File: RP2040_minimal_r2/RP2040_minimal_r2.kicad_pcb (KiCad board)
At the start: 2 copper layers, 52 x 51 mm, 34 parts, among them J1 USB_B_Micro, J2 Conn_01x02, J3 Conn_02x18_Odd_Even, J4 Conn_02x18_Odd_Even, U1 NCP1117-3.3_SOT223, U2 W25Q128JVS, U3 RP2040, Y1 ABM8-272-T3

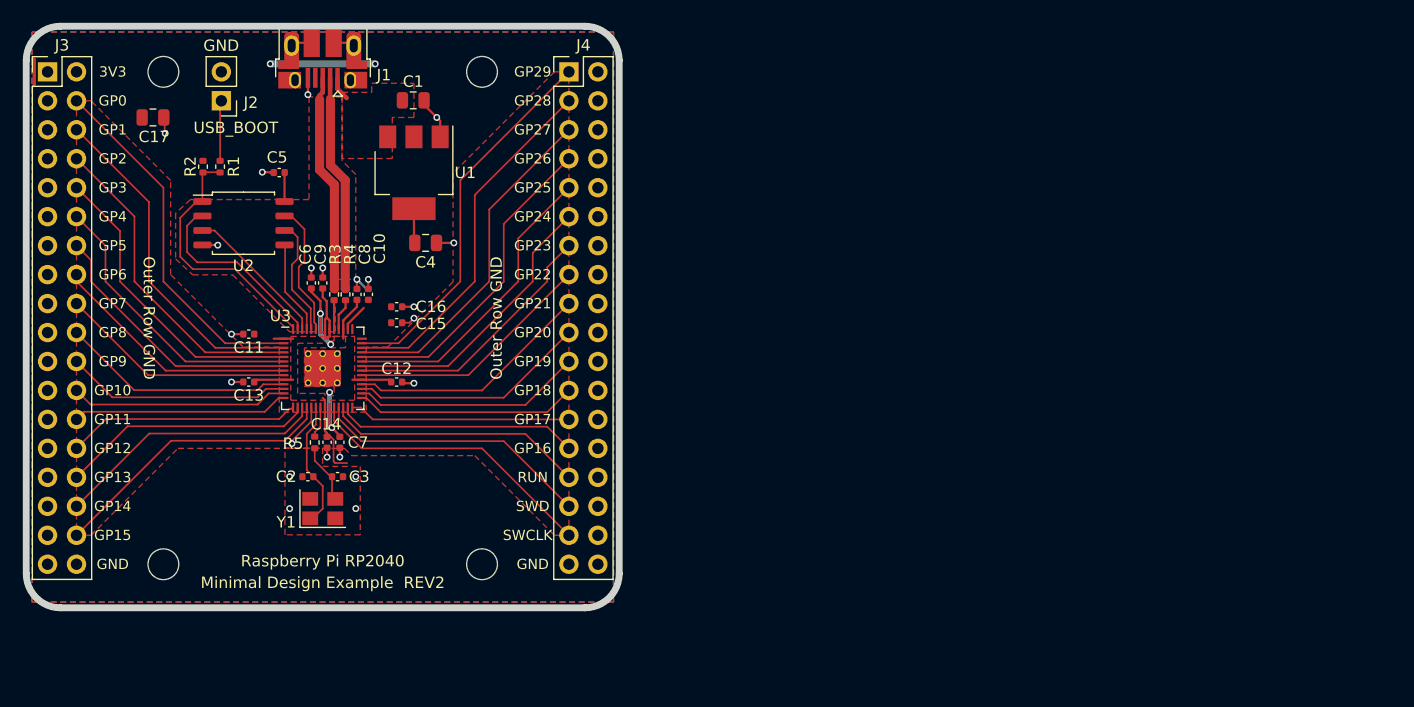
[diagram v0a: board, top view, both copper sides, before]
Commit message: Reshape board to 46x34mm to match the footprint of the old breadboard. Replace some components (voltage regulator, flash memory chip, crystal) with ones that are cheaper and/or smaller Add BOOT/RESET buttons Add SMD piezo speaker add 3 SPI connectors (JST-GH 1.25mm pitch 6 pin). Lots of routing etc.
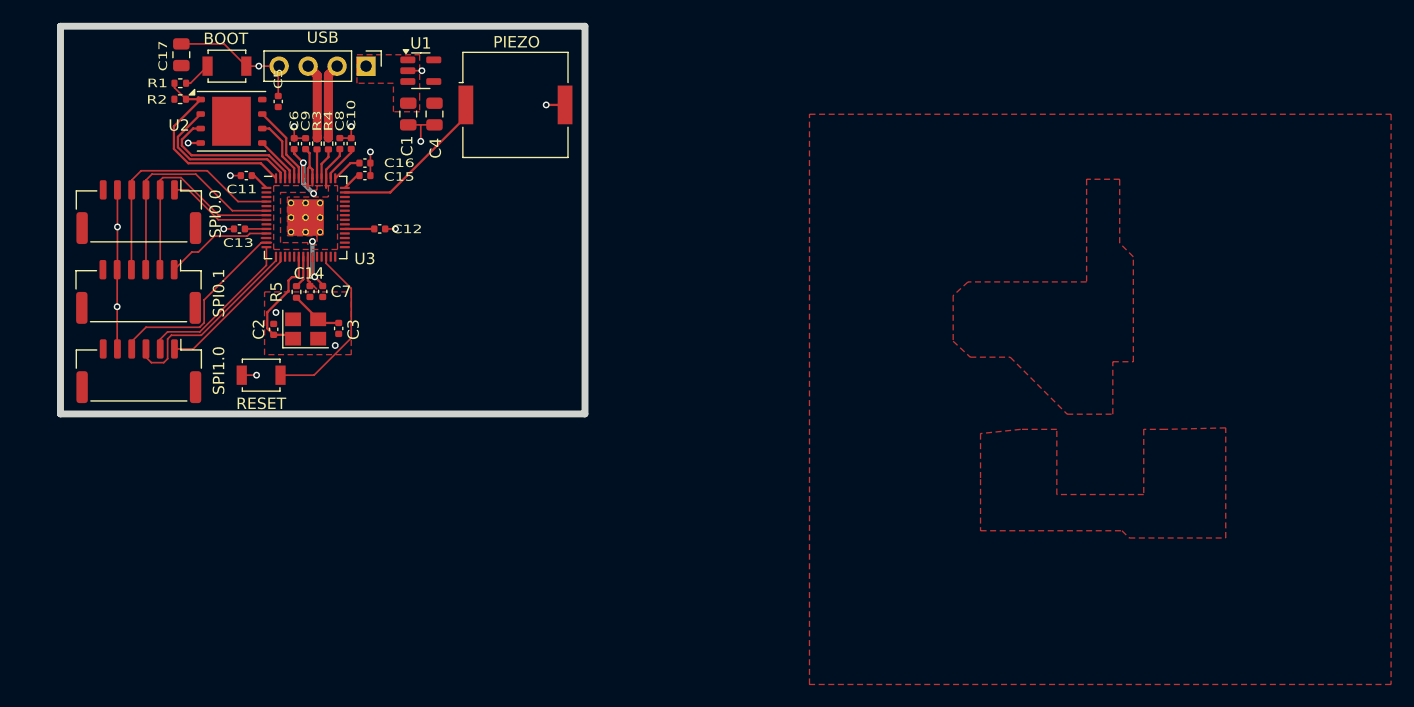
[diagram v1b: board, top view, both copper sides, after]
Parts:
- removed H1, H2, H3, H4: MountingHole, MountingHole:MountingHole_2.7mm_M2.5
- removed J4: Conn_02x18_Odd_Even, Connector_PinHeader_2.54mm:PinHeader_2x18_P2.54mm_Vertical
- added J5: USB, Connector_PinHeader_2.54mm:PinHeader_1x04_P2.54mm_Vertical, F.Cu at (103.8, 73.5)
- added LS1: PIEZO, Buzzer_Beeper:Buzzer_Murata_PKMCS0909E, F.Cu at (116.9, 76.9)
- added SW1: BOOT, Button_Switch_SMD:SW_SPST_B3U-1000P, F.Cu at (91.6, 73.5)
- added SW2: RESET, Button_Switch_SMD:SW_SPST_B3U-1000P, F.Cu at (94.6, 100.6)
- J1: value USB_B_Micro -> SPI0.0; footprint RP2040_minimal:USB_Micro-B_Amphenol_10103594-0001LF_Horizontal_modified -> Connector_JST:JST_GH_BM06B-GHS-TBT_1x06-1MP_P1.25mm_Vertical
- J2: value Conn_01x02 -> SPI0.1; footprint Connector_PinHeader_2.54mm:PinHeader_1x02_P2.54mm_Vertical -> Connector_JST:JST_GH_BM06B-GHS-TBT_1x06-1MP_P1.25mm_Vertical
- J3: value Conn_02x18_Odd_Even -> SPI1.0; footprint Connector_PinHeader_2.54mm:PinHeader_2x18_P2.54mm_Vertical -> Connector_JST:JST_GH_BM06B-GHS-TBT_1x06-1MP_P1.25mm_Vertical
- U1: value NCP1117-3.3_SOT223 -> AP2112K-3.3TRG1; footprint Package_TO_SOT_SMD:SOT-223-3_TabPin2 -> Package_TO_SOT_SMD:SOT-23-5
- U2: footprint Package_SO:SOIC-8_5.23x5.23mm_P1.27mm -> Package_SON:WSON-8-1EP_6x5mm_P1.27mm_EP3.4x4.3mm
- Y1: value ABM8-272-T3 -> X322512MSB4SI
- moved J3 27.4 mm to (83.9, 100.2), turned to 180 degrees
- moved J1 21.8 mm to (83.9, 86.3)
- moved J2 18.3 mm to (83.8, 93.3)
- moved Y1 15.8 mm to (98.5, 96.5)
- moved C11 13.9 mm to (93.3, 83.1)
- moved C12 13.5 mm to (105.0, 87.8)
- moved C13 13.4 mm to (92.7, 87.8)
- moved C10 13.3 mm to (102.5, 80.3)
- moved C14 13.3 mm to (98.9, 93.3)
- moved C7 13.3 mm to (100.0, 93.3)
- moved C8 13.3 mm to (101.5, 80.3)
- moved R3 13.3 mm to (99.5, 80.3)
- moved R4 13.3 mm to (100.5, 80.3)
- moved U3 13.3 mm to (98.5, 86.8)
- moved R5 13.3 mm to (97.7, 93.3)
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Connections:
- J1 pad 1: VBUS -> NCS0.0
- J1 pad 2: /USB_D- -> MOSI
- J1 pad 3: /USB_D+ -> MISO
- J1 pad 4: unconnected-(J1-ID-Pad4) -> SCLK
- J1 pad 6: GND -> +3V3
- J2 pad 1: /~{USB_BOOT} -> NCS0.1
- J2 pad 2: GND -> MOSI
- J3 pad 1: GND -> NCS1.0
- J3 pad 2: +3V3 -> MOSI1
- J3 pad 3: GND -> MISO1
- J3 pad 4: /GPIO0 -> SCLK1
- J3 pad 6: /GPIO1 -> +3V3
- R1 pad 2: /~{USB_BOOT} -> Net-(R1-Pad2)
- U1 pad 1: GND -> VBUS
- U1 pad 2: +3V3 -> GND
- U3 pad 11: /GPIO8 -> NCS0.1
- U3 pad 12: /GPIO9 -> unconnected-(U3-GPIO9-Pad12)
- U3 pad 13: /GPIO10 -> SCLK1
- U3 pad 14: /GPIO11 -> MOSI1
- U3 pad 15: /GPIO12 -> MISO1
- U3 pad 16: /GPIO13 -> NCS1.0
- U3 pad 17: /GPIO14 -> unconnected-(U3-GPIO14-Pad17)
- U3 pad 18: /GPIO15 -> unconnected-(U3-GPIO15-Pad18)
- U3 pad 2: /GPIO0 -> unconnected-(U3-GPIO0-Pad2)
- U3 pad 27: /GPIO16 -> unconnected-(U3-GPIO16-Pad27)
- U3 pad 28: /GPIO17 -> unconnected-(U3-GPIO17-Pad28)
- U3 pad 29: /GPIO18 -> unconnected-(U3-GPIO18-Pad29)
- U3 pad 3: /GPIO1 -> unconnected-(U3-GPIO1-Pad3)
- U3 pad 30: /GPIO19 -> unconnected-(U3-GPIO19-Pad30)
- U3 pad 31: /GPIO20 -> unconnected-(U3-GPIO20-Pad31)
- U3 pad 32: /GPIO21 -> unconnected-(U3-GPIO21-Pad32)
- U3 pad 34: /GPIO22 -> unconnected-(U3-GPIO22-Pad34)
- U3 pad 35: /GPIO23 -> unconnected-(U3-GPIO23-Pad35)
- U3 pad 36: /GPIO24 -> unconnected-(U3-GPIO24-Pad36)
- U3 pad 37: /GPIO25 -> unconnected-(U3-GPIO25-Pad37)
- U3 pad 38: /GPIO26_ADC0 -> unconnected-(U3-GPIO26_ADC0-Pad38)
- U3 pad 39: /GPIO27_ADC1 -> unconnected-(U3-GPIO27_ADC1-Pad39)
- U3 pad 4: /GPIO2 -> SCLK
- U3 pad 40: /GPIO28_ADC2 -> unconnected-(U3-GPIO28_ADC2-Pad40)
- U3 pad 41: /GPIO29_ADC3 -> /PIEZO
- U3 pad 5: /GPIO3 -> unconnected-(U3-GPIO3-Pad5)
- U3 pad 6: /GPIO4 -> MISO
- U3 pad 7: /GPIO5 -> MOSI
- U3 pad 8: /GPIO6 -> NCS0.0
- U3 pad 9: /GPIO7 -> unconnected-(U3-GPIO7-Pad9)
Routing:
- net /GPIO29_ADC3: track 33.2 -> 0.00 mm
- net /GPIO0: track 31.8 -> 0.00 mm
- net /GPIO28_ADC2: track 31.6 -> 0.00 mm
- net /GPIO1: track 30.2 -> 0.00 mm
- net /GPIO27_ADC1: track 29.9 -> 0.00 mm
- net /GPIO2: track 28.5 -> 0.00 mm
- net /GPIO26_ADC0: track 28.3 -> 0.00 mm
- net /GPIO3: track 26.9 -> 0.00 mm
- net /GPIO25: track 26.7 -> 0.00 mm
- net /SWCLK: track 25.9 -> 0.00 mm
- net /GPIO15: track 25.4 -> 0.00 mm
- net /GPIO4: track 25.3 -> 0.00 mm
- net /GPIO24: track 25.0 -> 0.00 mm
- net /SWD: track 24.3 -> 0.00 mm
- net /GPIO14: track 23.8 -> 0.00 mm
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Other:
- board size 52 x 51 mm -> 46 x 34 mm
- board text removed: "3V3"
- board text removed: "GND"
- board text removed: "GP0"
- board text removed: "GP1"
- board text removed: "GP10"
- board text removed: "GP11"
- board text removed: "GP12"
- board text removed: "GP13"
- board text removed: "GP14"
- board text removed: "GP15"
- board text removed: "GP16"
- board text removed: "GP17"
- board text removed: "GP18"
- board text removed: "GP19"
- board text removed: "GP2"
- board text removed: "GP20"
- board text removed: "GP21"
- board text removed: "GP22"
- board text removed: "GP23"
- board text removed: "GP24"
- board text removed: "GP25"
- board text removed: "GP26"
- board text removed: "GP27"
- board text removed: "GP28"
- board text removed: "GP29"
- board text removed: "GP3"
- board text removed: "GP4"
- board text removed: "GP5"
- board text removed: "GP6"
- board text removed: "GP7"
- board text removed: "GP8"
- board text removed: "GP9"
- board text removed: "Minimal Design Example REV2"
- board text removed: "Outer Row GND"
- board text removed: "RUN"
- board text removed: "Raspberry Pi RP2040"
- board text removed: "SWCLK"
- board text removed: "SWD"
- board text removed: "USB_BOOT"

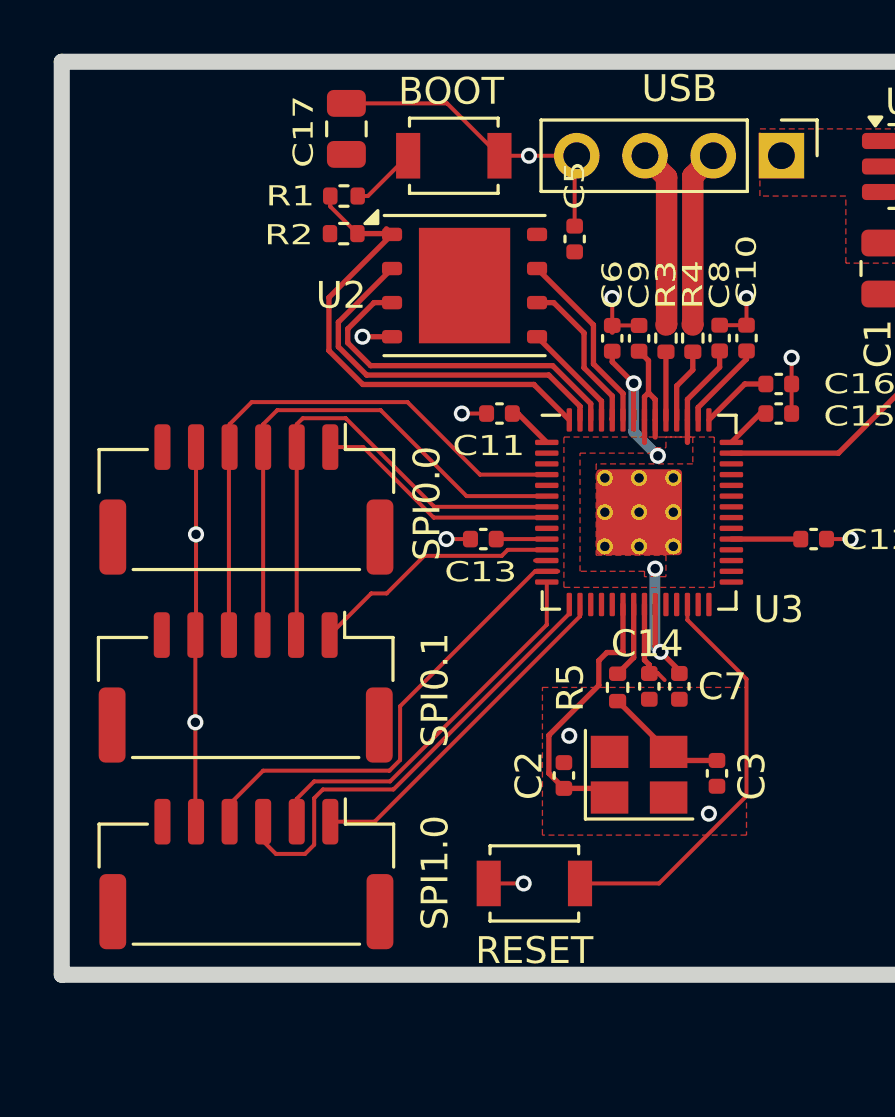
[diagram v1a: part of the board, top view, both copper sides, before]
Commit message: Change connectors to JST-SH 1.0mm Additional routing tweaks.
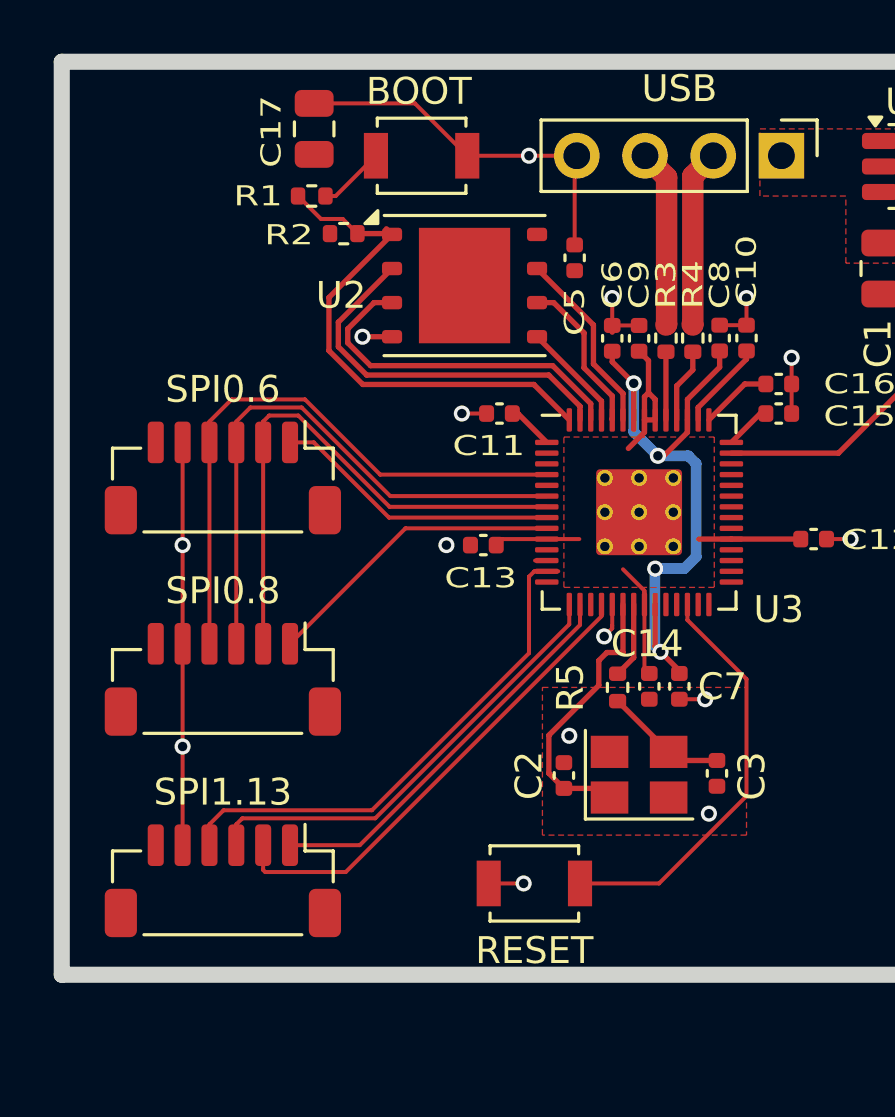
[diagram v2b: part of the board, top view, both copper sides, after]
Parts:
- J1: value SPI0.0 -> SPI0.6; footprint Connector_JST:JST_GH_BM06B-GHS-TBT_1x06-1MP_P1.25mm_Vertical -> Connector_JST:JST_SH_BM06B-SRSS-TB_1x06-1MP_P1.00mm_Vertical
- J2: value SPI0.1 -> SPI0.8; footprint Connector_JST:JST_GH_BM06B-GHS-TBT_1x06-1MP_P1.25mm_Vertical -> Connector_JST:JST_SH_BM06B-SRSS-TB_1x06-1MP_P1.00mm_Vertical
- J3: value SPI1.0 -> SPI1.13; footprint Connector_JST:JST_GH_BM06B-GHS-TBT_1x06-1MP_P1.25mm_Vertical -> Connector_JST:JST_SH_BM06B-SRSS-TB_1x06-1MP_P1.00mm_Vertical
- moved R1 1.20 mm to (86.3, 75.0)
- moved C17 1.20 mm to (86.4, 72.5)
- moved SW1 1.20 mm to (90.4, 73.5)
- moved J1 1.19 mm to (83.0, 85.5)
- moved J3 0.91 mm to (83.0, 100.5)
- moved J2 0.90 mm to (83.0, 93.0)
- moved C5 0.70 mm to (96.1, 77.3)
- moved C13 0.22 mm to (92.7, 88.0)
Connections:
- net NCS0.0 renamed NCS06
- net NCS1.0 renamed NCS13
- J2 pad 1: NCS0.1 -> NCS07
- U3 pad 11: NCS0.1 -> unconnected-(U3-GPIO8-Pad11)
- U3 pad 14: MOSI1 -> unconnected-(U3-GPIO11-Pad14)
- U3 pad 18: unconnected-(U3-GPIO15-Pad18) -> MOSI1
- U3 pad 9: unconnected-(U3-GPIO7-Pad9) -> NCS07
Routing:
- net NCS07: track 0.00 -> 11.3 mm
- net NCS0.1: track 9.40 -> 0.00 mm
- net +1V1: track 16.0 -> 23.8 mm
- net GND: track 44.5 -> 48.7 mm, vias 16 -> 18
- net MOSI1: track 14.4 -> 17.9 mm
- net +3V3: track 23.0 -> 26.3 mm
- net NCS13: track 12.9 -> 15.0 mm
- net SCLK1: track 17.7 -> 19.3 mm
- net MOSI: track 18.7 -> 20.3 mm
- net NCS06: track 9.15 -> 10.7 mm
- net MISO: track 20.0 -> 21.4 mm
- net SCLK: track 21.2 -> 22.3 mm
- net /QSPI_SS: track 19.0 -> 19.9 mm
- net MISO1: track 16.7 -> 17.3 mm
- removed copper zone on F.Cu, net +1V1

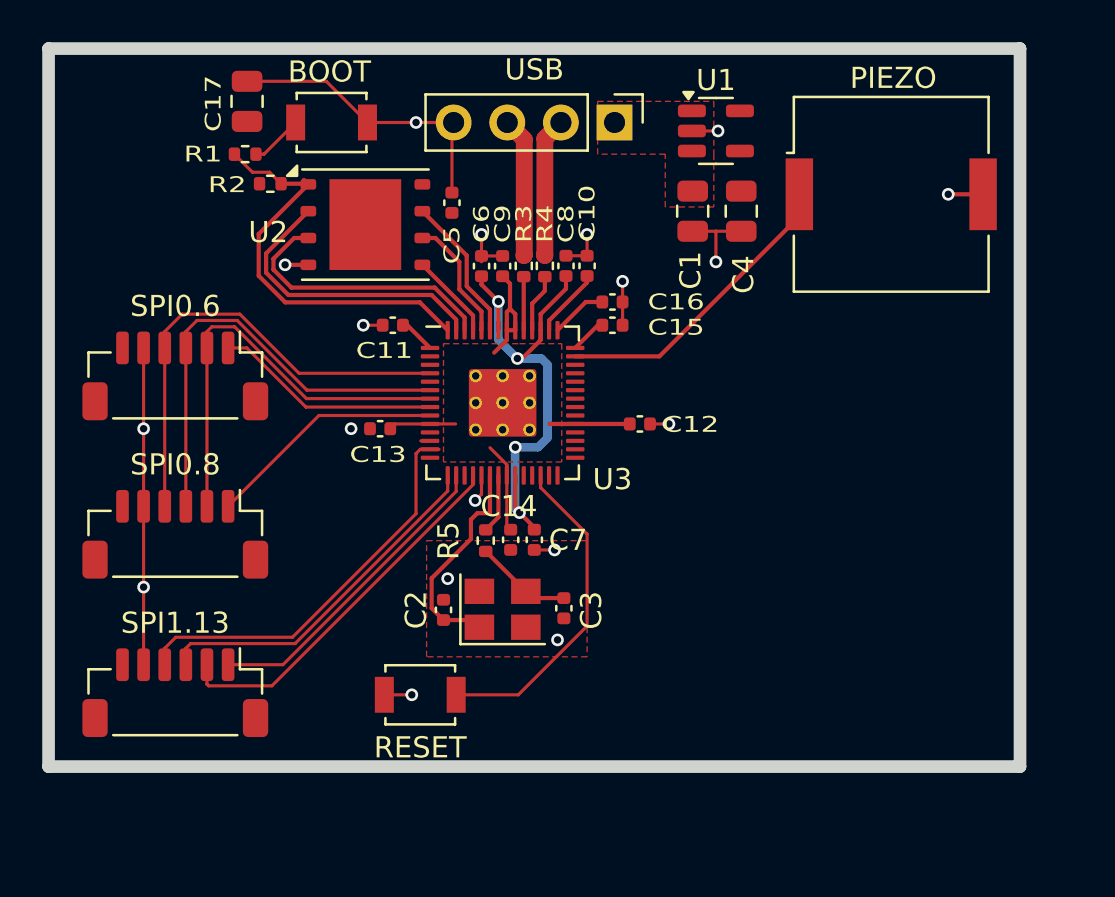
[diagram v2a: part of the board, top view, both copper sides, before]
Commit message: Add I2C/STEMMA QT connector
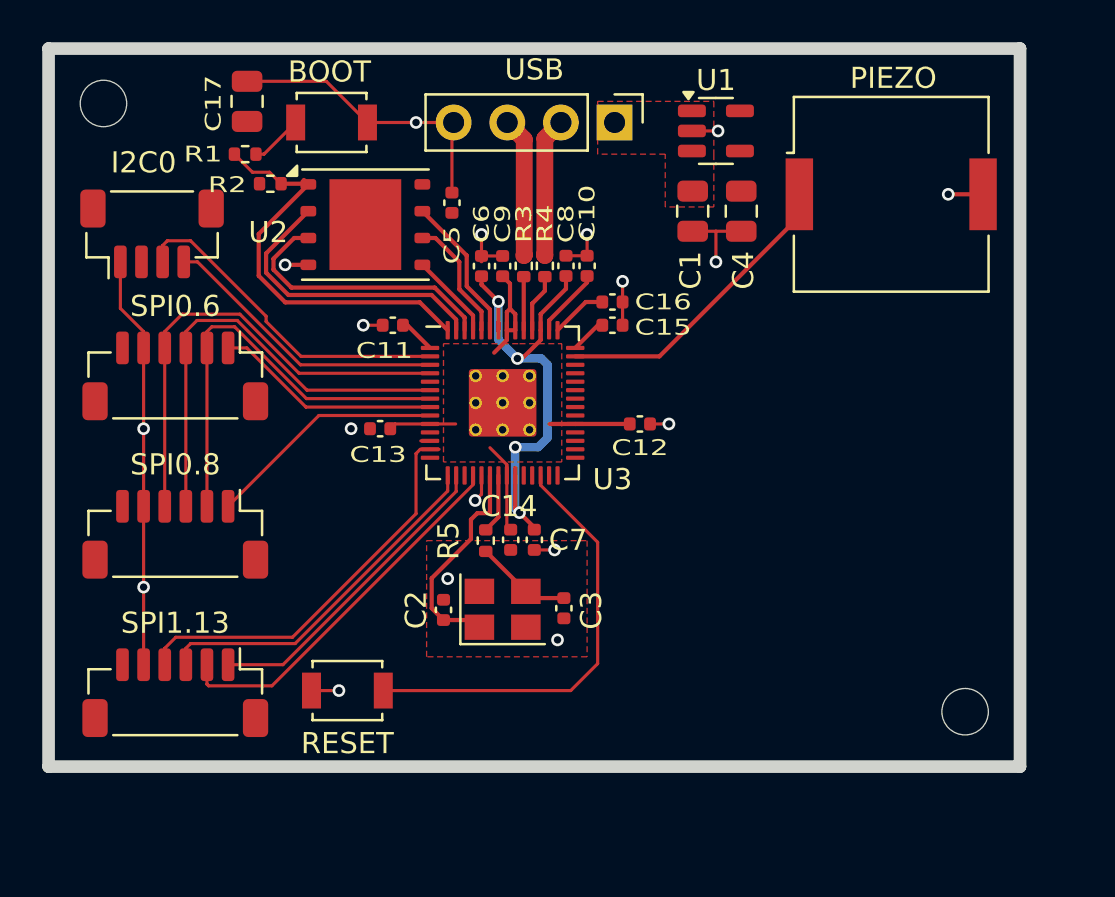
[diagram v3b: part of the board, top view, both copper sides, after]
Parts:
- added H1: MountingHole, MountingHole:MountingHole_2.2mm_M2, F.Cu at (79.6, 72.6)
- added H2: MountingHole, MountingHole:MountingHole_2.2mm_M2, F.Cu at (120.4, 101.4)
- added J4: I2C0, Connector_JST:JST_SH_BM04B-SRSS-TB_1x04-1MP_P1.00mm_Vertical, F.Cu at (81.9, 78.8)
- moved SW2 3.46 mm to (91.2, 100.4)
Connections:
- U3 pad 2: unconnected-(U3-GPIO0-Pad2) -> I2C0_SDA
- U3 pad 3: unconnected-(U3-GPIO1-Pad3) -> I2C0_SCL
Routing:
- net I2C0_SDA: track 0.00 -> 15.9 mm
- net I2C0_SCL: track 0.00 -> 13.7 mm
- net /RUN: track 15.6 -> 20.7 mm
- net GND: track 48.7 -> 53.3 mm
